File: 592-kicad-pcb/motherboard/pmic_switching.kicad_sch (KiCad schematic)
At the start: 10 parts

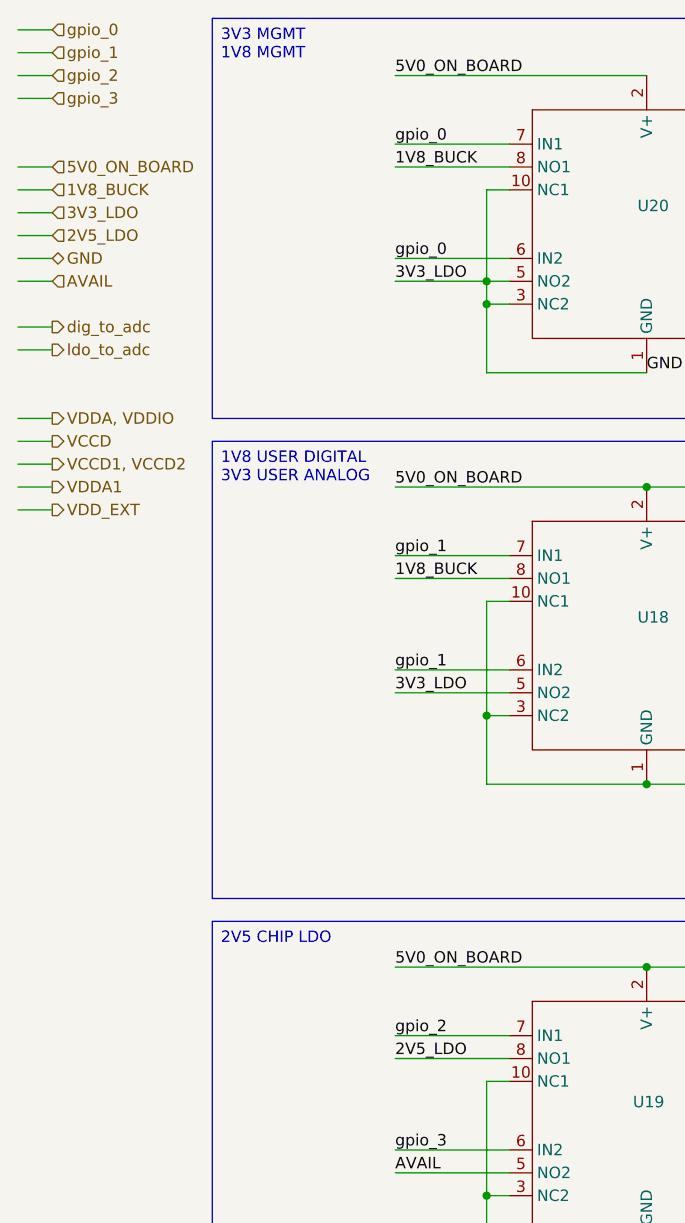
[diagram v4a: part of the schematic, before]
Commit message: supply connectors, solder bridges
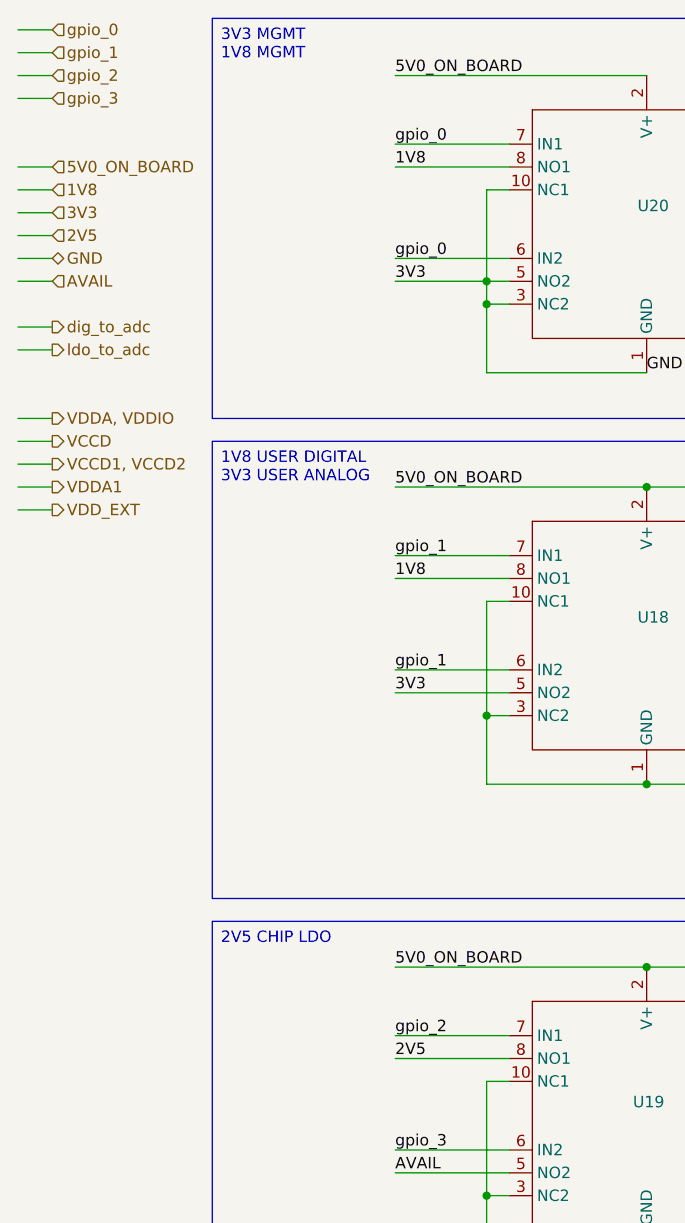
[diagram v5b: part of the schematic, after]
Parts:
- F2: value (none) -> ~
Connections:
- net 1V8_BUCK renamed 1V8
- net 2V5_LDO renamed 2V5
- net 3V3_LDO renamed 3V3
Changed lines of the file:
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@@
 		)
 	)
-	(label "3V3_LDO"
+	(label "3V3"
 		(at 58.42 88.9 0)
 		(effects
@@
 		)
 	)
-	(label "1V8_BUCK"
+	(label "1V8"
 		(at 58.42 30.48 0)
 		(effects
@@
 		)
 	)
-	(label "1V8_BUCK"
+	(label "1V8"
 		(at 58.42 76.2 0)
 		(effects
@@
 		)
 	)
-	(label "3V3_LDO"
+	(label "3V3"
 		(at 58.42 43.18 0)
 		(effects
@@
 		)
 	)
-	(label "2V5_LDO"
+	(label "2V5"
 		(at 58.42 129.54 0)
 		(effects
@@
 		)
 	)
-	(hierarchical_label "1V8_BUCK"
+	(hierarchical_label "1V8"
 		(shape input)
 		(at 20.32 33.02 0)
@@
 		)
 	)
-	(hierarchical_label "2V5_LDO"
+	(hierarchical_label "2V5"
 		(shape input)
 		(at 20.32 38.1 0)
@@
 		)
 	)
-	(hierarchical_label "3V3_LDO"
+	(hierarchical_label "3V3"
 		(shape input)
 		(at 20.32 35.56 0)
@@
 			)
 		)
-		(property "Value" ""
+		(property "Value" "~"
 			(at 137.16 159.258 90)
 			(effects
